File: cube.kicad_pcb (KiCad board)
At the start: 2 copper layers, 300 parts, among them J1 serial_conn, J10 Conn_01x01, J11 Conn_01x01, J2 shifters_common_conn, J3 Conn_01x01, J4 Conn_01x01, J5 Conn_01x01, J6 Conn_01x01, J7 Conn_01x01, J8 Conn_01x01, J9 Conn_01x01, Q1 IRF9540N, Q2 IRF9540N, Q3 IRF9540N, Q4 IRF9540N, Q5 IRF9540N, Q6 IRF9540N, Q7 IRF9540N, Q8 IRF9540N, U1 SN74HC595N_0_b, U10 SN74HC595N_3_b, U11 SN74HC595N_3_g, U12 SN74HC595N_3_r, U13 SN74HC595N_4_b, U14 SN74HC595N_4_g, U15 SN74HC595N_4_r, U16 SN74HC595N_5_b, U17 SN74HC595N_5_g, U18 SN74HC595N_5_r, U19 SN74HC595N_6_b, U2 SN74HC595N_0_g, U20 SN74HC595N_6_g, U21 SN74HC595N_6_r, U22 SN74HC595N_7_b, U23 SN74HC595N_7_g, U24 SN74HC595N_7_r, U25 SN74HC595N_cols, U3 SN74HC595N_0_r, U4 SN74HC595N_1_b, U5 SN74HC595N_1_g, U6 SN74HC595N_1_r, U7 SN74HC595N_2_b, U8 SN74HC595N_2_g, U9 SN74HC595N_2_r

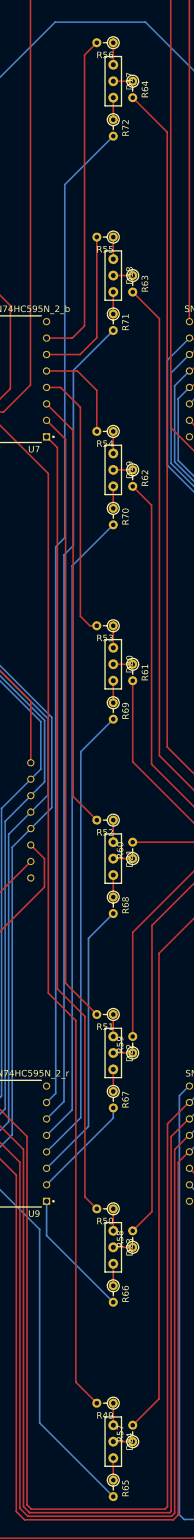
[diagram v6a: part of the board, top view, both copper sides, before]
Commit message: fix 3rd rows's red conns
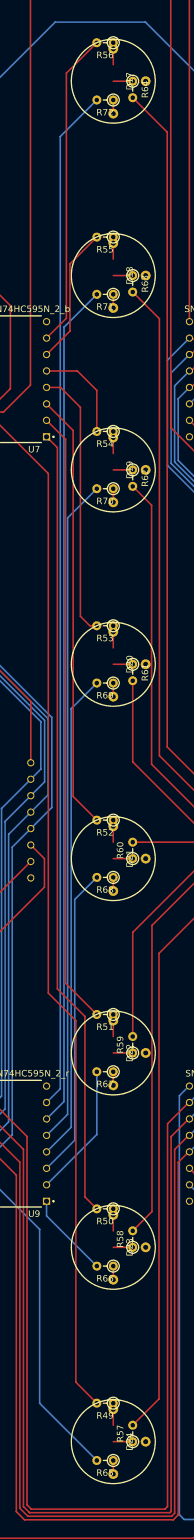
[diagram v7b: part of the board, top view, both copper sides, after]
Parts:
- moved R65 3.04 mm to (104.0, 302.9), turned to 180 degrees
- moved R66 3.04 mm to (104.0, 272.9), turned to 180 degrees
- moved R67 3.04 mm to (104.0, 242.9), turned to 180 degrees
- moved R68 3.04 mm to (104.0, 212.9), turned to 180 degrees
- moved R69 3.04 mm to (104.0, 182.9), turned to 180 degrees
- moved R70 3.04 mm to (104.0, 152.9), turned to 180 degrees
- moved R71 3.04 mm to (104.0, 122.9), turned to 180 degrees
- moved R72 3.04 mm to (104.0, 92.9), turned to 180 degrees
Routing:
- net Net-(R66-Pad2): track 19.9 -> 13.2 mm
- net Net-(R65-Pad2): track 55.7 -> 49.1 mm
- net Net-(R68-Pad2): track 43.6 -> 48.1 mm
- net Net-(R67-Pad2): track 16.1 -> 20.7 mm
- net Net-(R72-Pad2): track 153.4 -> 158.0 mm
- net Net-(R70-Pad2): track 98.5 -> 103.0 mm
- net Net-(R69-Pad2): track 71.1 -> 75.6 mm
- net Net-(R71-Pad2): track 126.0 -> 130.5 mm
- net Net-(R55-Pad2): track 24.4 -> 21.3 mm
- net Net-(R56-Pad2): track 51.1 -> 48.8 mm
- net led_2_5_r: track 3.40 -> 2.10 mm
- net led_2_4_r: track 3.40 -> 2.10 mm
- net led_2_3_r: track 3.40 -> 2.10 mm
- net led_2_2_r: track 3.40 -> 2.10 mm
- net led_2_1_r: track 3.40 -> 2.10 mm
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
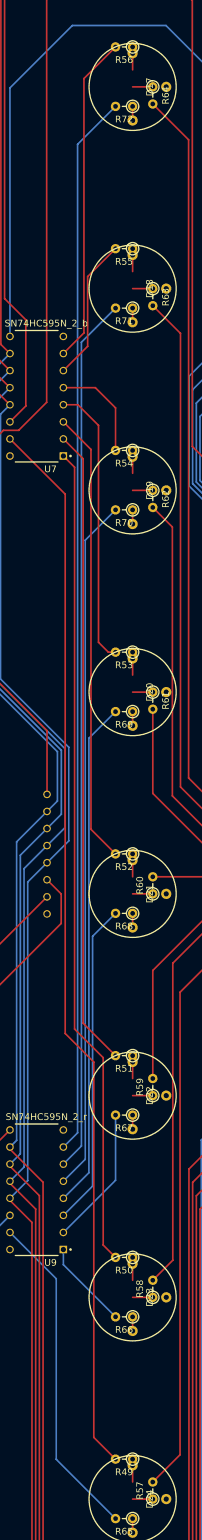
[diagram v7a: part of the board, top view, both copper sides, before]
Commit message: fix 3rd rows's blue conns
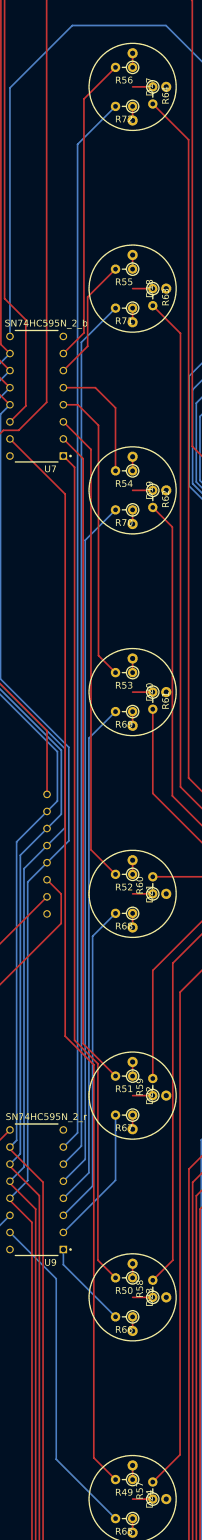
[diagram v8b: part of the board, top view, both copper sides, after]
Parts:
- moved R52 3.04 mm to (104.0, 207.1)
- moved R49 3.04 mm to (104.0, 297.1)
- moved R50 3.04 mm to (104.0, 267.1)
- moved R51 3.04 mm to (104.0, 237.1)
- moved R53 3.04 mm to (104.0, 177.1)
- moved R54 3.04 mm to (104.0, 147.1)
- moved R55 3.04 mm to (104.0, 117.1)
- moved R56 3.04 mm to (104.0, 87.1)
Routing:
- net Net-(R49-Pad2): track 158.3 -> 161.4 mm
- net Net-(R52-Pad2): track 67.5 -> 70.5 mm
- net Net-(R51-Pad2): track 94.9 -> 98.0 mm
- net Net-(R50-Pad2): track 122.4 -> 125.4 mm
- net Net-(R56-Pad2): track 48.8 -> 45.8 mm
- net Net-(R55-Pad2): track 21.3 -> 18.3 mm
- net Net-(R54-Pad2): track 15.3 -> 18.4 mm
- net Net-(R53-Pad2): track 41.9 -> 44.3 mm
- net led_2_5_b: track 3.40 -> 2.10 mm
- net led_2_4_b: track 3.40 -> 2.10 mm
- net led_2_3_b: track 3.40 -> 2.10 mm
- net led_2_2_b: track 3.40 -> 2.10 mm
- net led_2_1_b: track 3.40 -> 2.10 mm
- net led_2_0_b: track 3.40 -> 2.10 mm
- net led_2_7_b: track 3.40 -> 2.10 mm
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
